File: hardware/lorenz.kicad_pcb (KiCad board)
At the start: 2 copper layers, 100 x 100 mm, 54 parts, among them J1 USB-C, J2 BNC, J3 BNC, J4 BNC, SW1 SW_DIP_x06, U1 LF412, U2 LF412, U3 MPY634, U4 MPY634, U5 A0515S-2WR2, U6 78L12, U7 79L12

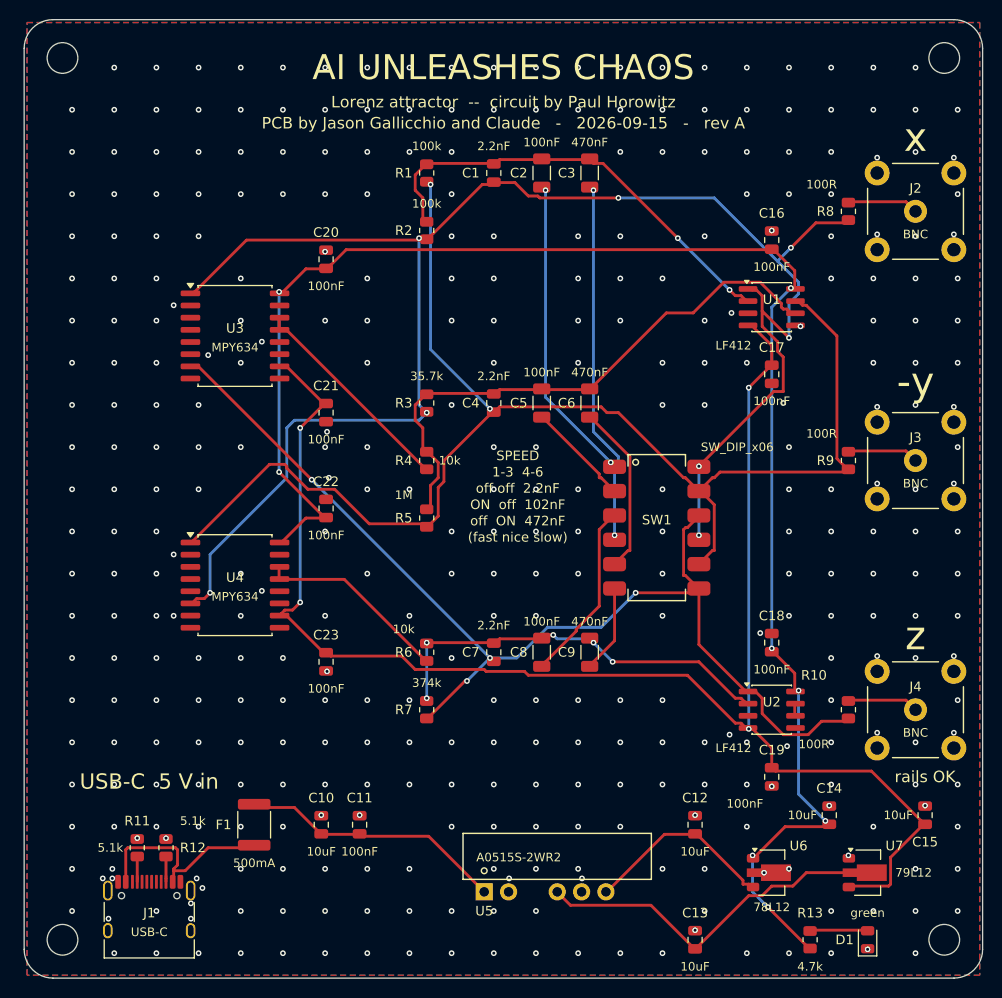
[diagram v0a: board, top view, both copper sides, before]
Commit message: Use the isolation, add a chaos lamp and probe pads, drop the four-layer board
Circuit
 * The converter's isolation is now used.  GND (everything a scope touches)
   and GNDU (the USB input and its shell) are separate copper pours with a
   1 mm gap, bridged only by R21 = 1 M, C25 = 2.2 nF and JP1, an open solder
   jumper marked GND TIE.  The point is the ground loop: scope earth -> BNC
   shell -> board ground -> USB cable -> laptop -> earth, landing on signals
   whose full scale is 2 V.  U5 straddles the gap with its own barrier over it.
 * A common-cathode RGB lamp driven by x, -y and z, with its cathode held at
   -1.50 V by the half of U2 Paul never needed.  Holding the cathode below
   ground is what lets signals that swing either side of zero drive an LED:
   each colour lights above its own threshold, so red marks the +x wing, green
   the -x wing and blue brightens with z.  Resistors sized for equal perceived
   brightness, not equal current.
 * Three rail lamps -- yellow +5 V, green +12 V, white -12 V -- replacing one
   green LED that claimed "rails OK" while knowing nothing about two of them.
   All three are JLCPCB Basic parts, so the colours cost nothing.
 * Thirteen probe pads, each carrying on the silkscreen the name of what it
   probes, and three wire loops for a scope's ground clip.  Deliberately none
   on the summing junctions: they are virtual earths whose voltage is zero by
   construction, and a probe there is a 15 us pole on the integrator's input.

Board
 * The four-layer variant is gone.  Measured on the routed board: tracks cover
   1.2 % of the back copper, so the pour is already 98.8 % of an unbroken
   ground plane, against four times the bare-board price.
 * Two QR codes on the back, drawn by scripts/qrcode_gen.py, whose data
   placement and Reed-Solomon match the 'qrcode' package module for module and
   whose mask scoring matches segno's; check_outputs.py decodes them back out
   of the finished board on every build.
 * The switch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
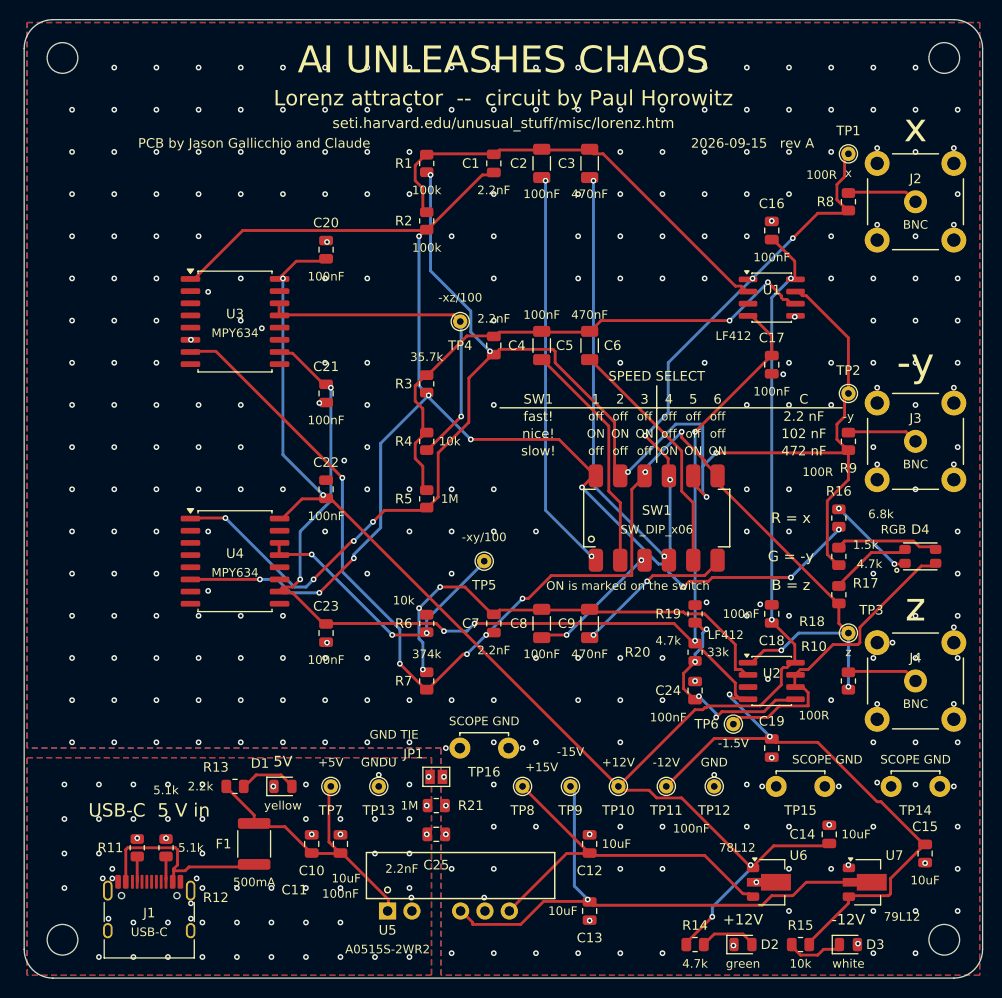
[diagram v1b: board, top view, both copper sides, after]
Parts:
- added C24: 100nF, Capacitor_SMD:C_0805_2012Metric, F.Cu at (70.0, 70.0)
- added C25: 2.2nF, Capacitor_SMD:C_0805_2012Metric, F.Cu at (43.0, 85.0)
- added D2: green, LED_SMD:LED_0805_2012Metric, F.Cu at (75.0, 96.5)
- added D3: white, LED_SMD:LED_0805_2012Metric, F.Cu at (86.0, 96.5)
- added D4: RGB, lorenz:LED_RGB_PLCC4_3.5x2.8mm, F.Cu at (93.5, 56.0)
- added JP1: GND TIE, Jumper:SolderJumper-2_P1.3mm_Open_Pad1.0x1.5mm, F.Cu at (43.0, 79.0)
- added R14: 4.7k, Resistor_SMD:R_0805_2012Metric, F.Cu at (70.0, 96.5)
- added R15: 10k, Resistor_SMD:R_0805_2012Metric, F.Cu at (81.0, 96.5)
- added R16: 1.5k, Resistor_SMD:R_0805_2012Metric, F.Cu at (85.0, 52.0)
- added R17: 6.8k, Resistor_SMD:R_0805_2012Metric, F.Cu at (85.0, 56.0)
- added R18: 4.7k, Resistor_SMD:R_0805_2012Metric, F.Cu at (85.0, 60.0)
- added R19: 4.7k, Resistor_SMD:R_0805_2012Metric, F.Cu at (70.0, 62.0)
- added R20: 33k, Resistor_SMD:R_0805_2012Metric, F.Cu at (70.0, 66.0)
- added R21: 1M, Resistor_SMD:R_0805_2012Metric, F.Cu at (43.0, 82.0)
- added TP1: x, TestPoint:TestPoint_THTPad_D1.5mm_Drill0.7mm, F.Cu at (86.0, 14.0)
- added TP10: +12V, TestPoint:TestPoint_THTPad_D1.5mm_Drill0.7mm, F.Cu at (62.0, 80.0)
- added TP11: -12V, TestPoint:TestPoint_THTPad_D1.5mm_Drill0.7mm, F.Cu at (67.0, 80.0)
- added TP12: GND, TestPoint:TestPoint_THTPad_D1.5mm_Drill0.7mm, F.Cu at (72.0, 80.0)
- added TP13: GNDU, TestPoint:TestPoint_THTPad_D1.5mm_Drill0.7mm, F.Cu at (37.0, 80.0)
- added TP14: SCOPE GND, lorenz:ScopeGround_Loop, F.Cu at (93.0, 80.0)
- added TP15: SCOPE GND, lorenz:ScopeGround_Loop, F.Cu at (81.0, 80.0)
- added TP16: SCOPE GND, lorenz:ScopeGround_Loop, F.Cu at (48.0, 76.0)
- added TP2: -y, TestPoint:TestPoint_THTPad_D1.5mm_Drill0.7mm, F.Cu at (86.0, 39.0)
- added TP3: z, TestPoint:TestPoint_THTPad_D1.5mm_Drill0.7mm, F.Cu at (86.0, 64.0)
- added TP4: -xz/100, TestPoint:TestPoint_THTPad_D1.5mm_Drill0.7mm, F.Cu at (45.5, 31.5)
- added TP5: -xy/100, TestPoint:TestPoint_THTPad_D1.5mm_Drill0.7mm, F.Cu at (48.0, 56.5)
- added TP6: -1.5V, TestPoint:TestPoint_THTPad_D1.5mm_Drill0.7mm, F.Cu at (74.0, 73.5)
- added TP7: +5V, TestPoint:TestPoint_THTPad_D1.5mm_Drill0.7mm, F.Cu at (32.0, 80.0)
- added TP8: +15V, TestPoint:TestPoint_THTPad_D1.5mm_Drill0.7mm, F.Cu at (52.0, 80.0)
- added TP9: -15V, TestPoint:TestPoint_THTPad_D1.5mm_Drill0.7mm, F.Cu at (57.0, 80.0)
- D1: value green -> yellow
- R13: value 4.7k -> 2.2k
- moved D1 63.1 mm to (27.0, 80.0), turned to 0 degrees
- moved R13 62.1 mm to (22.0, 80.0), turned to 0 degrees
- moved C13 11.4 mm to (59.0, 93.0)
- moved C12 11.2 mm to (59.0, 86.0)
- moved U5 10.3 mm to (37.9, 93.0)
- moved C4 6.00 mm to (49.0, 34.0)
- moved C5 6.00 mm to (54.0, 34.0)
- moved C6 6.00 mm to (59.0, 34.0)
- moved C15 4.00 mm to (94.0, 87.0)
- moved C18 3.00 mm to (78.0, 62.0)
- moved C19 3.00 mm to (78.0, 76.0)
- moved C23 3.00 mm to (31.5, 64.0)
- moved C7 3.00 mm to (49.0, 63.0)
- moved C8 3.00 mm to (54.0, 63.0)
- moved C9 3.00 mm to (59.0, 63.0)
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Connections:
- net Net-(U1A--) renamed /SJ_X
- net Net-(U1B--) renamed /SJ_Y
- net Net-(U2A--) renamed /SJ_Z
- C10 pad 2: GND -> GNDU
- C11 pad 2: GND -> GNDU
- C13 pad 1: -15V -> GND
- C13 pad 2: GND -> -15V
- C15 pad 1: -12V -> GND
- C15 pad 2: GND -> -12V
- D1 pad 1: GND -> GNDU
- J1 pad A1: GND -> GNDU
- J1 pad A12: GND -> GNDU
- J1 pad B1: GND -> GNDU
- J1 pad B12: GND -> GNDU
- J1 pad SH: GND -> GNDU
- R11 pad 2: GND -> GNDU
- R12 pad 2: GND -> GNDU
- R13 pad 1: +12V -> +5V
- U2 pad 5: GND -> Net-(U2B-+)
- U5 pad 2: GND -> GNDU
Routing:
- net Net-(D4-K): track 1.37 -> 33.3 mm
- net /x: track 181.9 -> 207.7 mm, vias 8 -> 14
- net Net-(U2B-+): track 0.00 -> 23.0 mm, vias 0 -> 4
- net /z: track 114.5 -> 137.3 mm, vias 4 -> 9
- net /-y: track 143.9 -> 165.3 mm, vias 2 -> 9
- net -15V: track 36.3 -> 56.3 mm, vias 0 -> 1
- net +15V: track 20.3 -> 39.6 mm
- net -12V: track 165.1 -> 183.4 mm, vias 4 -> 8
- net +12V: track 172.1 -> 190.0 mm, vias 8 -> 6
- net Net-(C5-Pad1): track 11.0 -> 24.3 mm
- net /xz: track 22.6 -> 35.4 mm, vias 0 -> 1
- net Net-(D4-G): track 0.00 -> 10.7 mm
- net /xy: track 20.1 -> 30.3 mm, vias 0 -> 3
- net Net-(C2-Pad1): track 32.3 -> 42.3 mm
- net Net-(D4-R): track 0.00 -> 9.40 mm, vias 0 -> 2
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- added copper zone on B.Cu, net GNDU
- added copper zone on F.Cu, net GNDU
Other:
- board text added: "+12V"
- board text added: "-12V"
- board text added: "1"
- board text added: "102 nF"
- board text added: "2"
- board text added: "2.2 nF"
- board text added: "3"
- board text added: "4"
- board text added: "472 nF"
- board text added: "5"
- board text added: "5V"
- board text added: "6"
- board text added: "A*B/10 and get their minus signs"
- board text added: "B = z"
- board text added: "C"
- board text added: "Every term weighs 1 MEG / R: R1 ="
- board text added: "G = -y"
- board text added: "ON"
- board text added: "ON is marked on the switch"
- board text added: "PCB by Jason Gallicchio and Claude 2026-09-15 rev A"
- board text added: "Paul's original:"
- board text added: "R = x"
- board text added: "R2 = 100k is s, R3 = 35.7k is r,"
- board text added: "R7 = 374k is b. The MPY634s form"
- board text added: "SPEED SELECT"
- board text added: "SW1"
- board text added: "fast!"
- board text added: "from swapped inputs. 0.1 V per unit,"
- board text added: "github.com/gallicchio"
- board text added: "nice!"
- board text added: "off"
- board text added: "seti.harvard.edu"
- board text added: "seti.harvard.edu/unusual_stuff/misc/lorenz.htm"
- board text added: "slow!"
- board text added: "this project:"
- board text added: "time scale tau = 1 MEG x C."
- board text added: "x and z on a scope in X-Y draw this"
- board text removed: "(fast nice slow)"
- board text removed: "1-3 4-6"
- board text removed: "100k gives s = 10, R3 = 35.7k gives r = 28.01,"
- board text removed: "Each op-amp integrates one derivative, and"
- board text removed: "ON off 102nF"
- board text removed: "PCB by Jason Gallicchio and Claude - 2026-09-15 - rev A"
- board text removed: "R7 = 374k gives b = 2.674. The two MPY634s"
- board text removed: "SPEED"
- board text removed: "at 0.1 V per unit. Time scale: tau = 1 MEG x C."
- board text removed: "every term is weighted 1 MEG / R: R1 = R2 ="
- board text removed: "form A*B/10 and get their minus signs from"
- board text removed: "off ON 472nF"
- board text removed: "off off 2.2nF"
- board text removed: "rails OK"
- board text removed: "swapped inputs. Signals carry the variables"
- board text removed: "x and z on a scope in X-Y draw this:"

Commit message: Rebuild the board around the multipliers, and review the whole design
Layout.  The multipliers move to the far left, into the third of the board
that was empty, and everything spreads out behind them.  Each output row is
now one straight line -- op-amp, probe pad, the 100 ohm lying horizontally,
BNC -- so what the probe pad is for needs no explaining.  The switch legend
gets clear board around it, both multipliers and both op-amps say what they
are, the chaos lamp has its own quarter with its resistors coming in from the
left, and the two QR codes are 62 mm apart with no drilled hole in either.

The lamp is redrawn: each colour is fed from its own integrator's *output*
node, tapped between the op-amp and the 100 ohm series resistor and brought
down the right margin, so there is no way to read it as current taken from an
op-amp input.  The three rail lamps are gone -- the chaos lamp cannot light
unless every rail is up, so it is the power-on indicator.

Review.  Four bugs, worst first.  DRC had never read this project's design
rules: pcbnew writes a default .kicad_pro beside any board it saves and
make.py only put the real one back after DRC ran, so every "0 violations" was
measured against KiCad's defaults.  The real rules turned up 203 violations.
Then: every via was 0.15 mm of annulus against a 0.25 mm rule; stitching vias
were leaving 0.08 mm necks of copper beside through-hole pads, which are
their own vias anyway; and the legend placer avoided pads but not package
bodies, so both multipliers had their designators printed underneath them.

New checks that run every build: check_pinout.py writes each IC's pin table
from its datasheet, compares it with the symbol used here, and compares it
again with KiCad's own library where the same part exists; gen_pcb.py refuses
to build if any net has pads on both sides of the isolation gap or any track
crosses it.  Four 100 nF parts now sit at the regulators' own pins, which is
what those datasheets are characterised with.

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
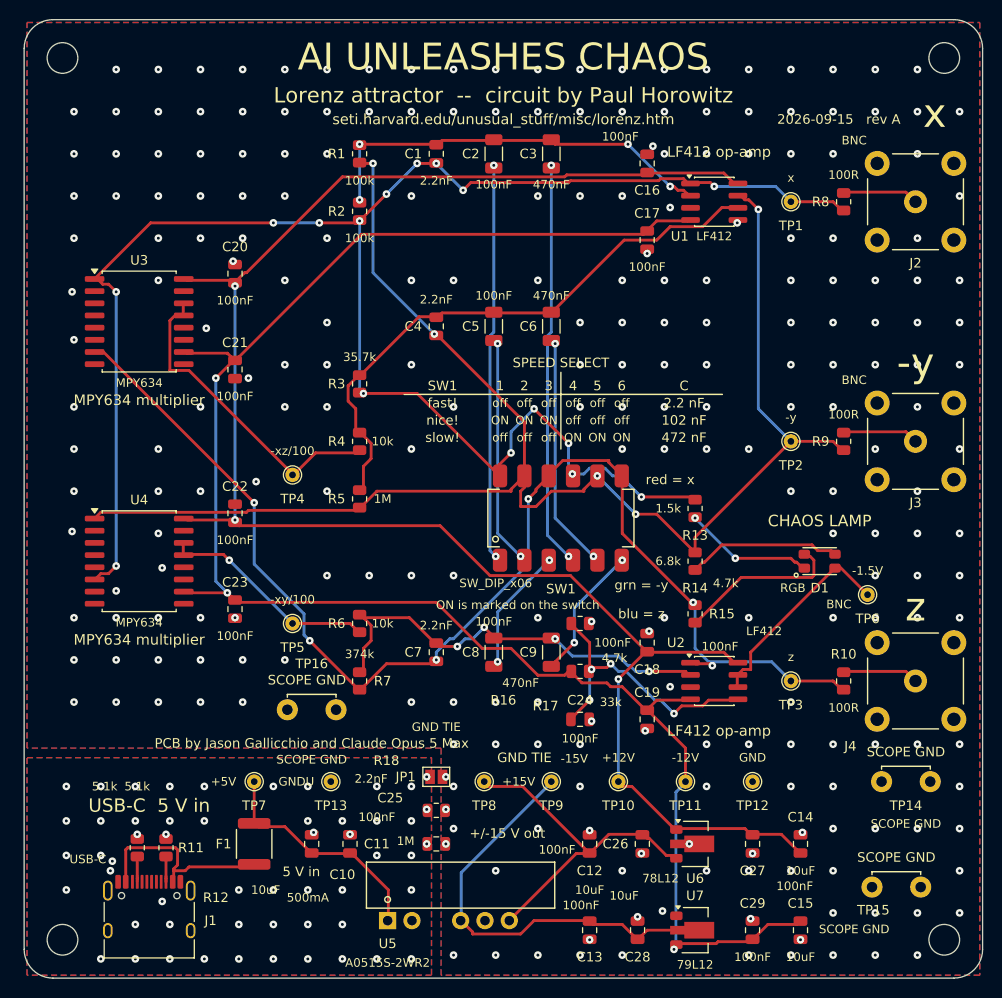
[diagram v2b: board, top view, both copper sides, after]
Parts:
- removed D2: green, LED_SMD:LED_0805_2012Metric
- removed D3: white, LED_SMD:LED_0805_2012Metric
- removed D4: RGB, lorenz:LED_RGB_PLCC4_3.5x2.8mm
- removed R19: 4.7k, Resistor_SMD:R_0805_2012Metric
- removed R20: 33k, Resistor_SMD:R_0805_2012Metric
- removed R21: 1M, Resistor_SMD:R_0805_2012Metric
- added C26: 100nF, Capacitor_SMD:C_0805_2012Metric, F.Cu at (64.5, 86.0)
- added C27: 100nF, Capacitor_SMD:C_0805_2012Metric, F.Cu at (76.0, 86.0)
- added C28: 100nF, Capacitor_SMD:C_0805_2012Metric, F.Cu at (64.0, 95.0)
- added C29: 100nF, Capacitor_SMD:C_0805_2012Metric, F.Cu at (76.0, 95.0)
- D1: value yellow -> RGB; footprint LED_SMD:LED_0805_2012Metric -> lorenz:LED_RGB_PLCC4_3.5x2.8mm
- F1: footprint Fuse:Fuse_1812_4532Metric -> lorenz:PTC_1812_4532Metric
- R13: value 2.2k -> 1.5k
- R14: value 4.7k -> 6.8k
- R15: value 10k -> 4.7k
- R16: value 1.5k -> 4.7k
- R17: value 6.8k -> 33k
- R18: value 4.7k -> 1M
- TP14, TP15, TP16: footprint lorenz:ScopeGround_Loop -> lorenz:TestPoint_ScopeGnd_Loop_2x1.1mm
- moved D1 60.7 mm to (83.0, 56.5)
- moved R13 56.1 mm to (70.0, 51.0), turned to 90 degrees
- moved R18 47.6 mm to (43.0, 82.5), turned to 0 degrees
- moved R14 40.0 mm to (70.0, 56.5), turned to 90 degrees
- moved R15 36.2 mm to (70.0, 62.0), turned to 90 degrees
- moved R17 29.5 mm to (58.0, 68.0), turned to 0 degrees
- moved R16 29.2 mm to (58.0, 63.0), turned to 0 degrees
- moved TP4 23.7 mm to (28.0, 47.5)
- moved TP5 21.0 mm to (28.0, 63.0)
- moved TP6 19.4 mm to (88.0, 60.0)
- moved U7 18.7 mm to (70.0, 95.0)
- moved TP16 18.4 mm to (30.0, 72.0)
- moved C17 18.4 mm to (65.0, 23.0)
- moved C15 15.3 mm to (81.0, 95.0)
- moved C16 14.8 mm to (65.0, 15.0)
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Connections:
- D1 pad 1: GNDU -> Net-(D1-R)
- D1 pad 2: Net-(D1-A) -> Net-(D1-B)
- R13 pad 1: +5V -> Net-(D1-R)
- R13 pad 2: Net-(D1-A) -> /x
- R14 pad 1: +12V -> Net-(D1-G)
- R14 pad 2: Net-(D2-A) -> /-y
- R15 pad 1: Net-(D3-K) -> Net-(D1-B)
- R15 pad 2: -12V -> /z
- R16 pad 1: /x -> Net-(U2B-+)
- R16 pad 2: Net-(D4-R) -> GND
- R17 pad 1: /-y -> -12V
- R17 pad 2: Net-(D4-G) -> Net-(U2B-+)
- R18 pad 1: /z -> GNDU
- R18 pad 2: Net-(D4-B) -> GND
- TP6 pad 1: Net-(D4-K) -> Net-(D1-K)
- U2 pad 6: Net-(D4-K) -> Net-(D1-K)
- U2 pad 7: Net-(D4-K) -> Net-(D1-K)
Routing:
- net Net-(D4-K): track 33.3 -> 0.00 mm
- net Net-(D1-K): track 0.00 -> 21.7 mm
- net /x: track 207.7 -> 188.4 mm, vias 14 -> 16
- net Net-(D1-B): track 0.00 -> 17.2 mm
- net Net-(D1-G): track 0.00 -> 16.1 mm
- net Net-(D1-R): track 0.00 -> 13.6 mm, vias 0 -> 2
- net -15V: track 56.3 -> 43.4 mm, vias 1 -> 0
- net Net-(D4-G): track 10.7 -> 0.00 mm
- net Net-(D4-R): track 9.40 -> 0.00 mm, vias 2 -> 0
- net Net-(D4-B): track 8.47 -> 0.00 mm
- net Net-(U2B-+): track 23.0 -> 30.9 mm
- net /xy: track 30.3 -> 23.0 mm, vias 3 -> 1
- net +5V: track 31.0 -> 24.4 mm
- net Net-(D3-K): track 6.05 -> 0.00 mm
- net Net-(D1-A): track 6.02 -> 0.00 mm
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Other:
- board text added: "+/-15 V out"
- board text added: "100k is s, R3 = 35.7k is r, R7 = 374k is b."
- board text added: "5 V in"
- board text added: "CHAOS LAMP"
- board text added: "Every term weighs 1 MEG / R: R1 = R2 ="
- board text added: "GND TIE"
- board text added: "LF412 op-amp"
- board text added: "MPY634 multiplier"
- board text added: "PCB by Jason Gallicchio and Claude Opus 5 Max"
- board text added: "PCB by Jason Gallicchio and Claude Opus 5 Max 2026-09-15 rev A"
- board text added: "Paul's original circuit"
- board text added: "SCOPE GND"
- board text added: "The MPY634s form A*B/10 and take their"
- board text added: "blu = z"
- board text added: "grn = -y"
- board text added: "it was made"
- board text added: "minus signs from swapped inputs. 0.1 V"
- board text added: "per unit; time scale tau = 1 MEG x C."
- board text added: "red = x"
- board text added: "this project, and how"
- board text removed: "+12V"
- board text removed: "-12V"
- board text removed: "5V"
- board text removed: "A*B/10 and get their minus signs"
- board text removed: "B = z"
- board text removed: "Every term weighs 1 MEG / R: R1 ="
- board text removed: "G = -y"
- board text removed: "PCB by Jason Gallicchio and Claude"
- board text removed: "PCB by Jason Gallicchio and Claude 2026-09-15 rev A"
- board text removed: "Paul's original:"
- board text removed: "R = x"
- board text removed: "R2 = 100k is s, R3 = 35.7k is r,"
- board text removed: "R7 = 374k is b. The MPY634s form"
- board text removed: "from swapped inputs. 0.1 V per unit,"
- board text removed: "github.com/gallicchio"
- board text removed: "this project:"
- board text removed: "time scale tau = 1 MEG x C."
